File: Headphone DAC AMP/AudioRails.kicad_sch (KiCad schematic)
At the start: 35 parts, among them U12 TPS74501PDRVR, U14 ADP7185ACPZN-R7, U2 TPS7A39

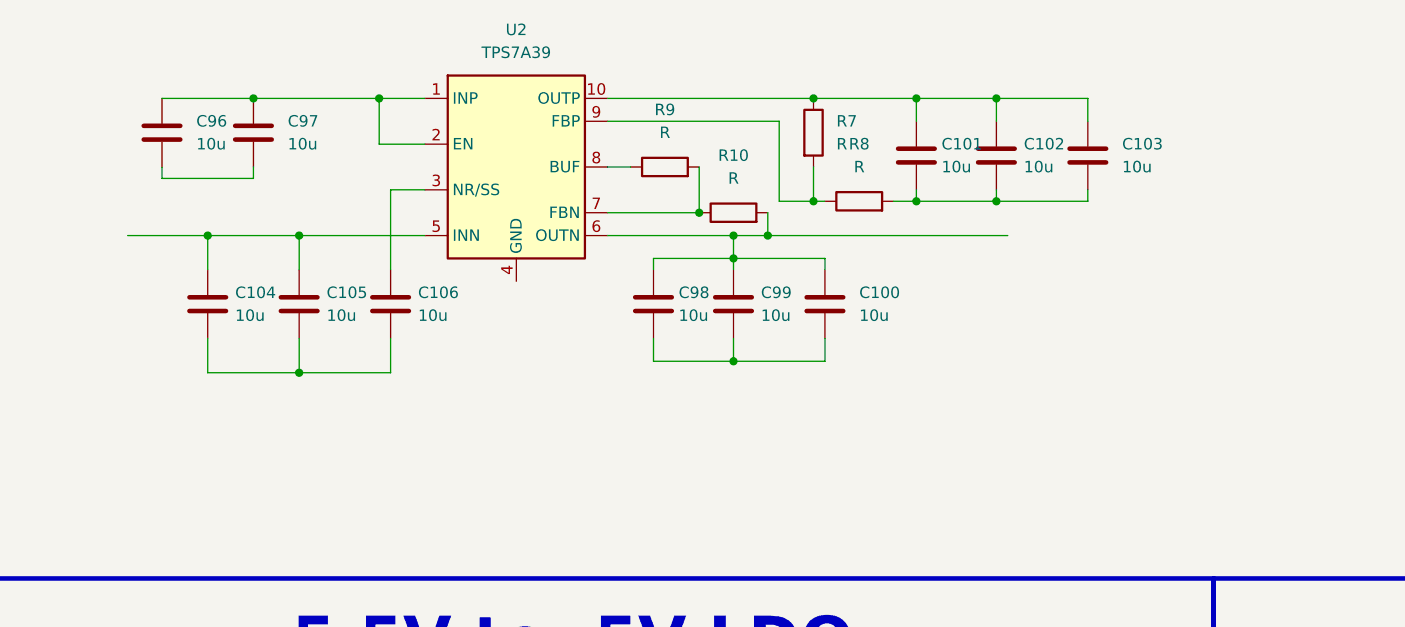
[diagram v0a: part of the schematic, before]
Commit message: Update schematic connections and add backup files
Added new junctions and wires to AudioRails.kicad_sch, updated connections for improved signal routing, and removed/re-added backup zip files. Also updated related schematic files to reflect new connections and organization.
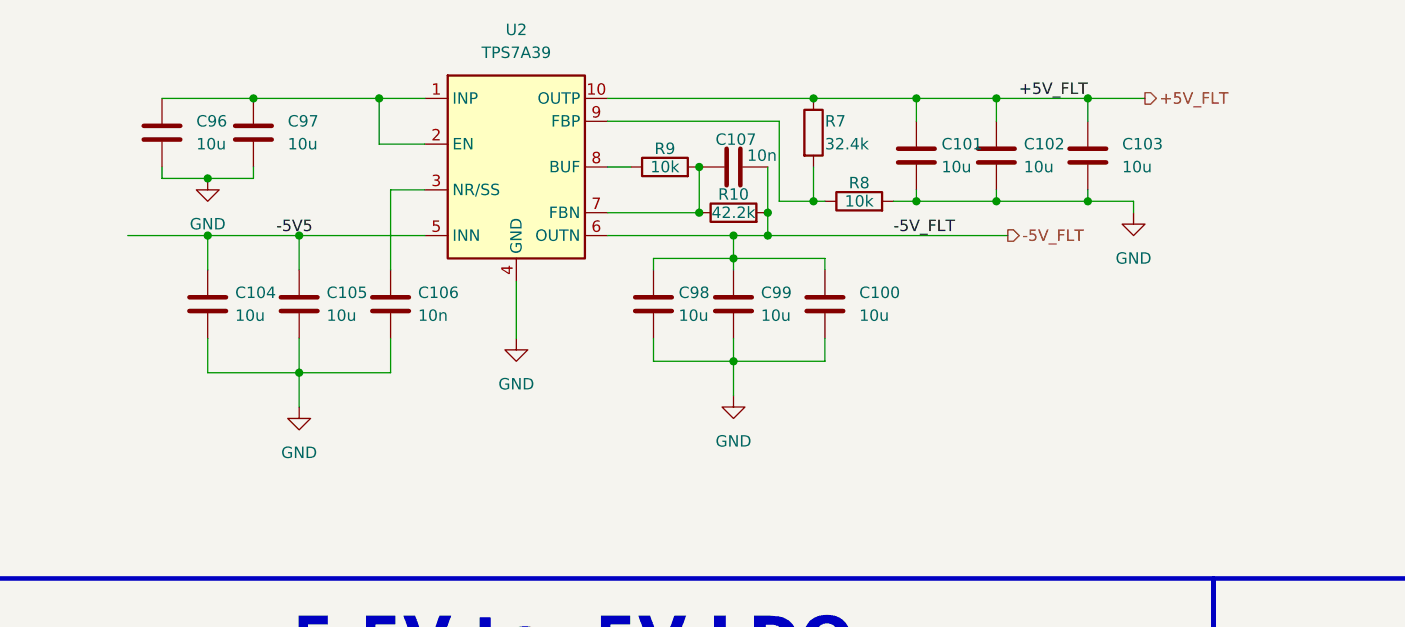
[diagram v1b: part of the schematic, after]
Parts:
- added C107: 10n, Capacitor_SMD:C_0603_1608Metric_Pad1.08x0.95mm_HandSolder, symbol Device:C
- C106: value 10u -> 10n
- R10: value R -> 42.2k
- R7: value R -> 32.4k
- R8, R9: value R -> 10k
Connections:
- net +5V_FLT: now also C101.1, C102.1, C103.1, R7.1, U2.10 (OUTP)
- net -5V5: now also C104.1, C105.1, U2.5 (INN)
- net -5V_FLT: now also C100.1, C98.1, C99.1, R10.2, U2.6 (OUTN), C107.2
- net GND: now also C100.2, C101.2, C102.2, C103.2, C104.2, C105.2, C106.2, C96.2, C97.2, C98.2, C99.2, R8.2, U2.11 (GND), U2.4 (GND)
- net at R10.1, R9.2, U2.7 (FBN): now also C107.1

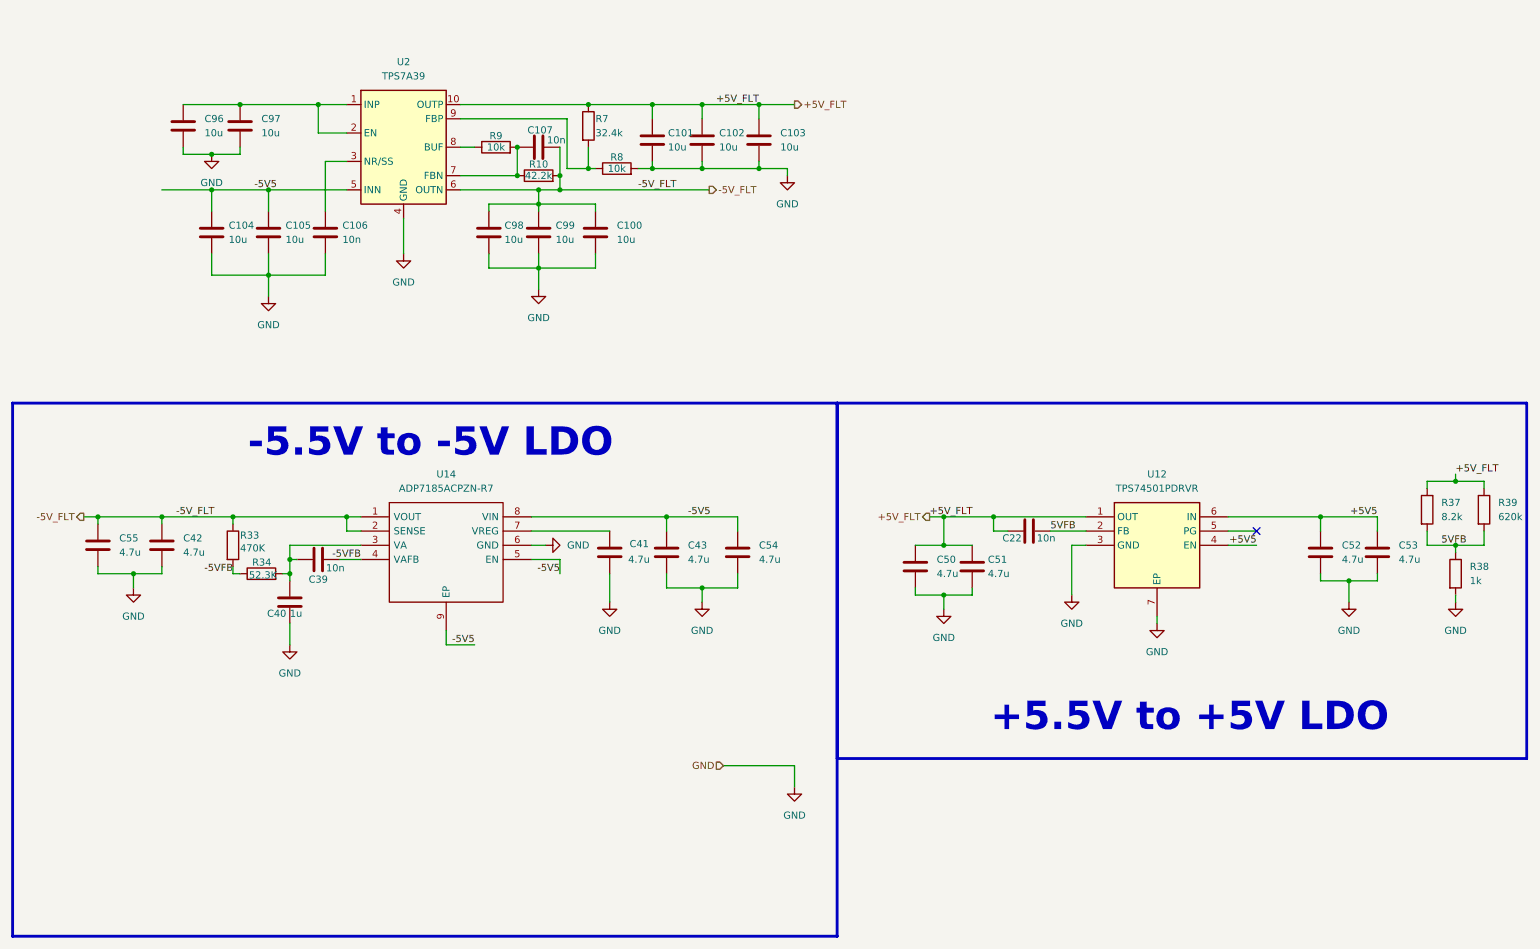
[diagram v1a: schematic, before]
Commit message: Refactor AudioRails schematic for new LDO and layout
Removed ADP7185 and TPS74501 LDO symbols and related wiring, updated power rail text to '+-6V to +-5V LDO', and significantly simplified the schematic layout and wiring by replacing the two seperate regulators with a single TPS7A39.
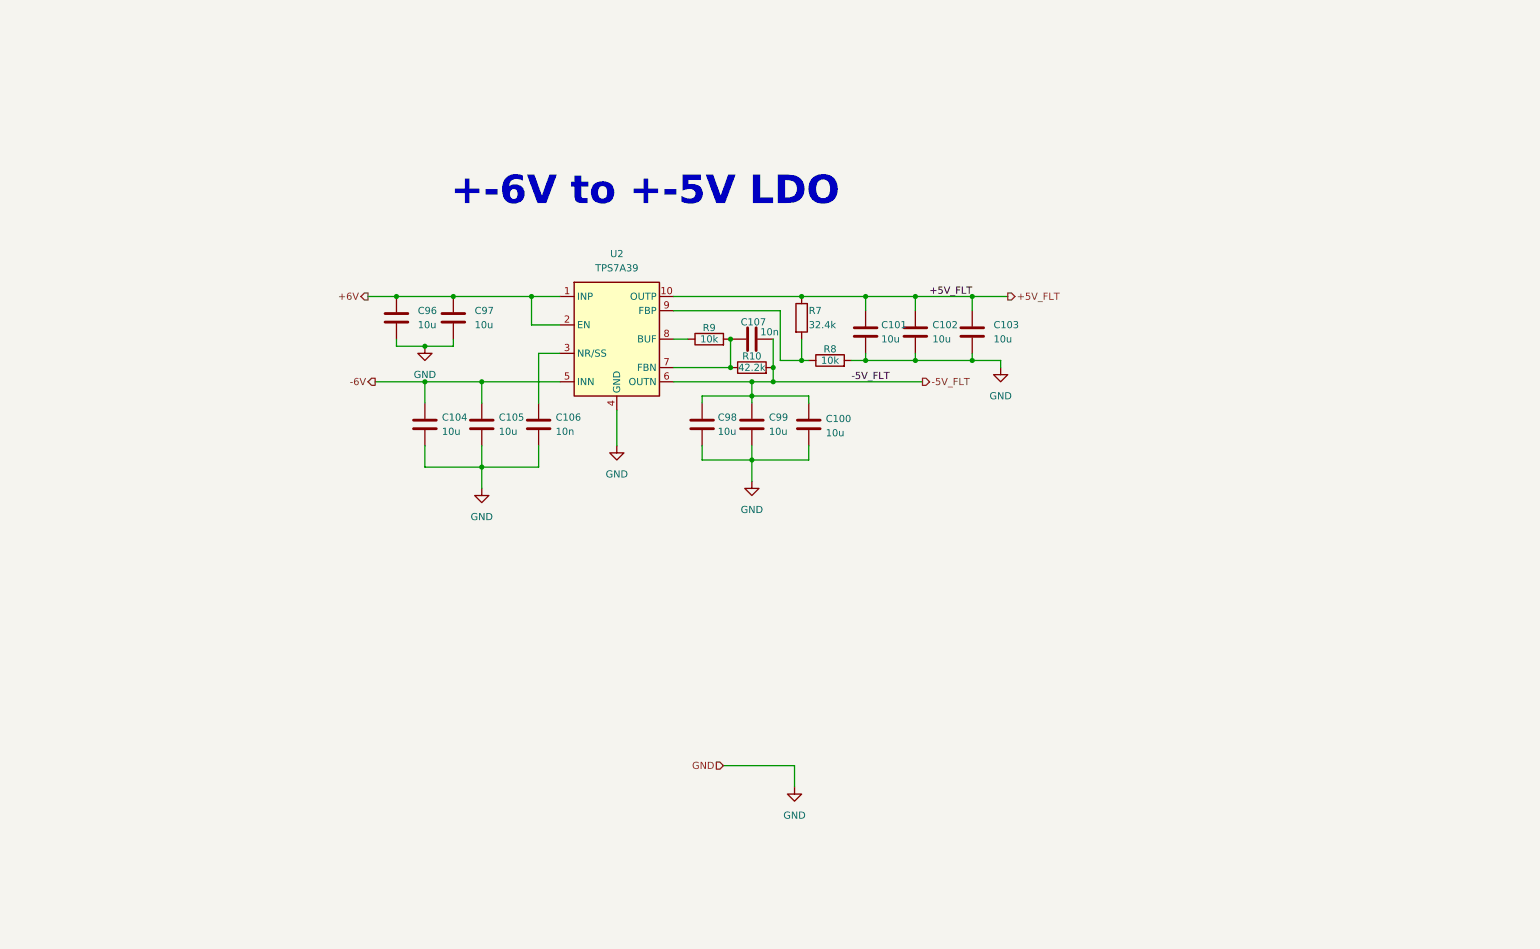
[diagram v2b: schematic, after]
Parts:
- removed C22, C39: 10n, Capacitor_SMD:C_0402_1005Metric_Pad0.74x0.62mm_HandSolder, symbol Device:C
- removed C40: 1u, Capacitor_SMD:C_0603_1608Metric_Pad1.08x0.95mm_HandSolder, symbol Device:C
- removed C41, C42, C43, C50, C51, C52, C53, C54, C55: 4.7u, Capacitor_SMD:C_0603_1608Metric_Pad1.08x0.95mm_HandSolder, symbol Device:C
- removed R33: 470K, Resistor_SMD:R_0805_2012Metric_Pad1.20x1.40mm_HandSolder, symbol Device:R
- removed R34: 52.3K, Resistor_SMD:R_0805_2012Metric_Pad1.20x1.40mm_HandSolder, symbol Device:R
- removed R37: 8.2k, Resistor_SMD:R_0805_2012Metric_Pad1.20x1.40mm_HandSolder, symbol Device:R
- removed R38: 1k, Resistor_SMD:R_0805_2012Metric_Pad1.20x1.40mm_HandSolder, symbol Device:R
- removed R39: 620k, Resistor_SMD:R_0805_2012Metric_Pad1.20x1.40mm_HandSolder, symbol Device:R
- removed U12: TPS74501PDRVR, TPS74501PDRVR:SON65P200X200X80-7N, symbol TPS74501PDRVR:TPS74501PDRVR
- removed U14: ADP7185ACPZN-R7, ADP7185ACPZN-R7:SON50P200X200X60-9N, symbol ADP7185ACPZN-R7:ADP7185ACPZN-R7
- R10, R7, R8, R9: footprint (none) -> Resistor_SMD:R_0805_2012Metric
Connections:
- net +6V: now reaches C96.1, C97.1, U2.1 (INP), U2.2 (EN)
- net -5V5 renamed -6V
- no-connect marks 1 -> 0
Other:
- note added: "+-6V to +-5V LDO"
- note removed: "+5.5V to +5V LDO"
- note removed: "-5.5V to -5V LDO"
- moved on the sheet: C100, C101, C102, C103, C104, C105, C106, C107, C96, C97, C98, C99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

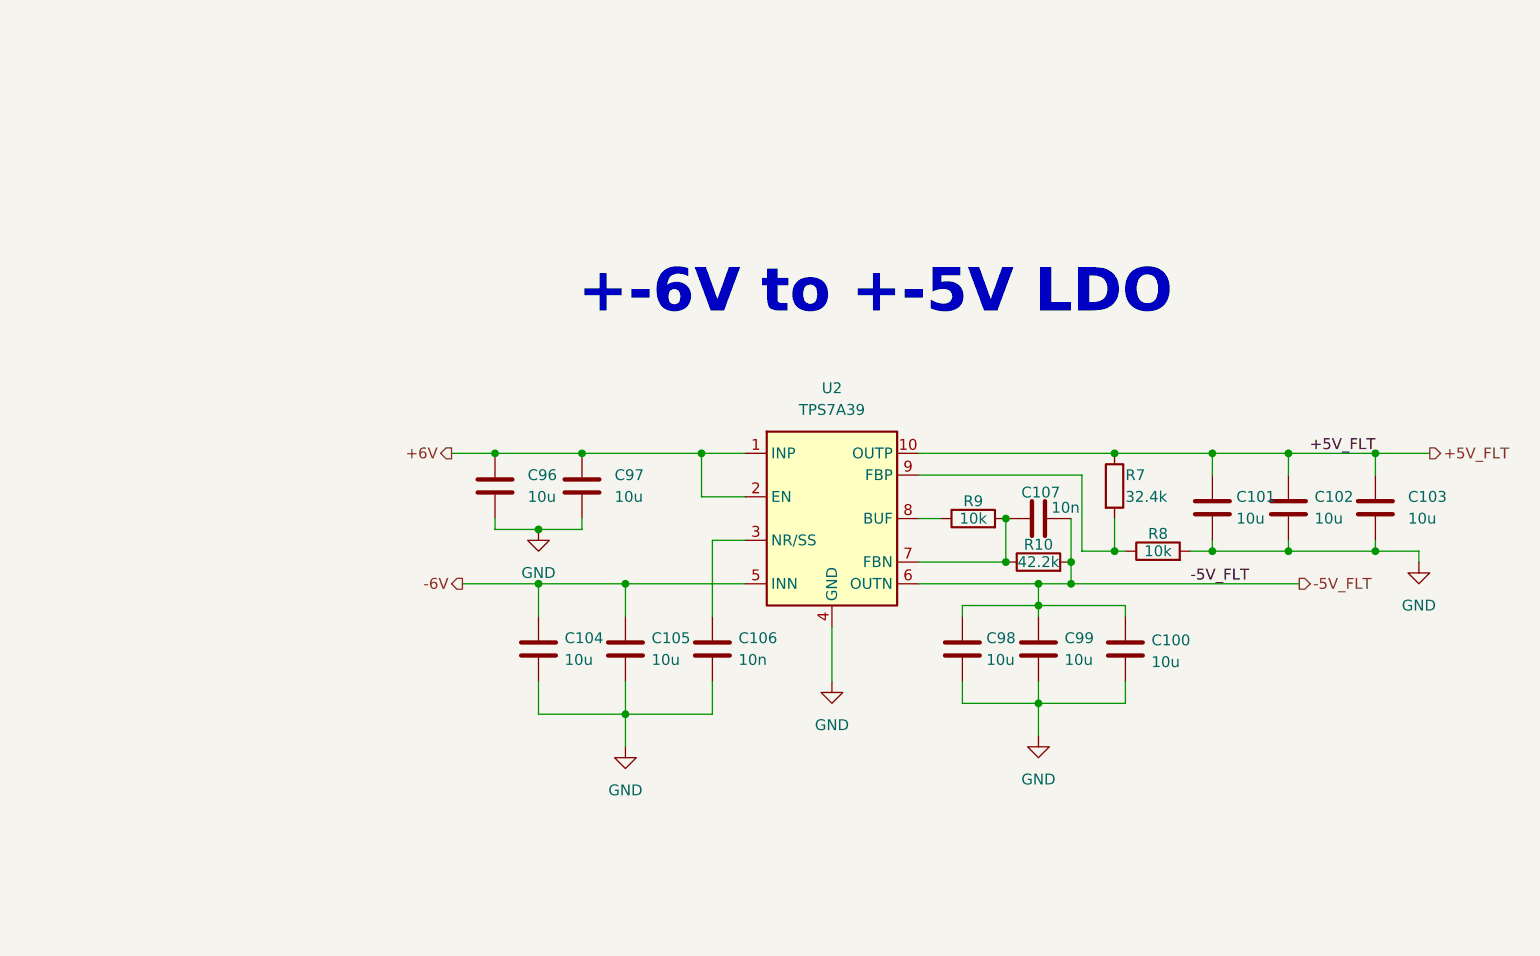
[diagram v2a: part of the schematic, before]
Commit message: dID lAYOUT FOR THE DIFFERENTIAL OUTPUT RAILS
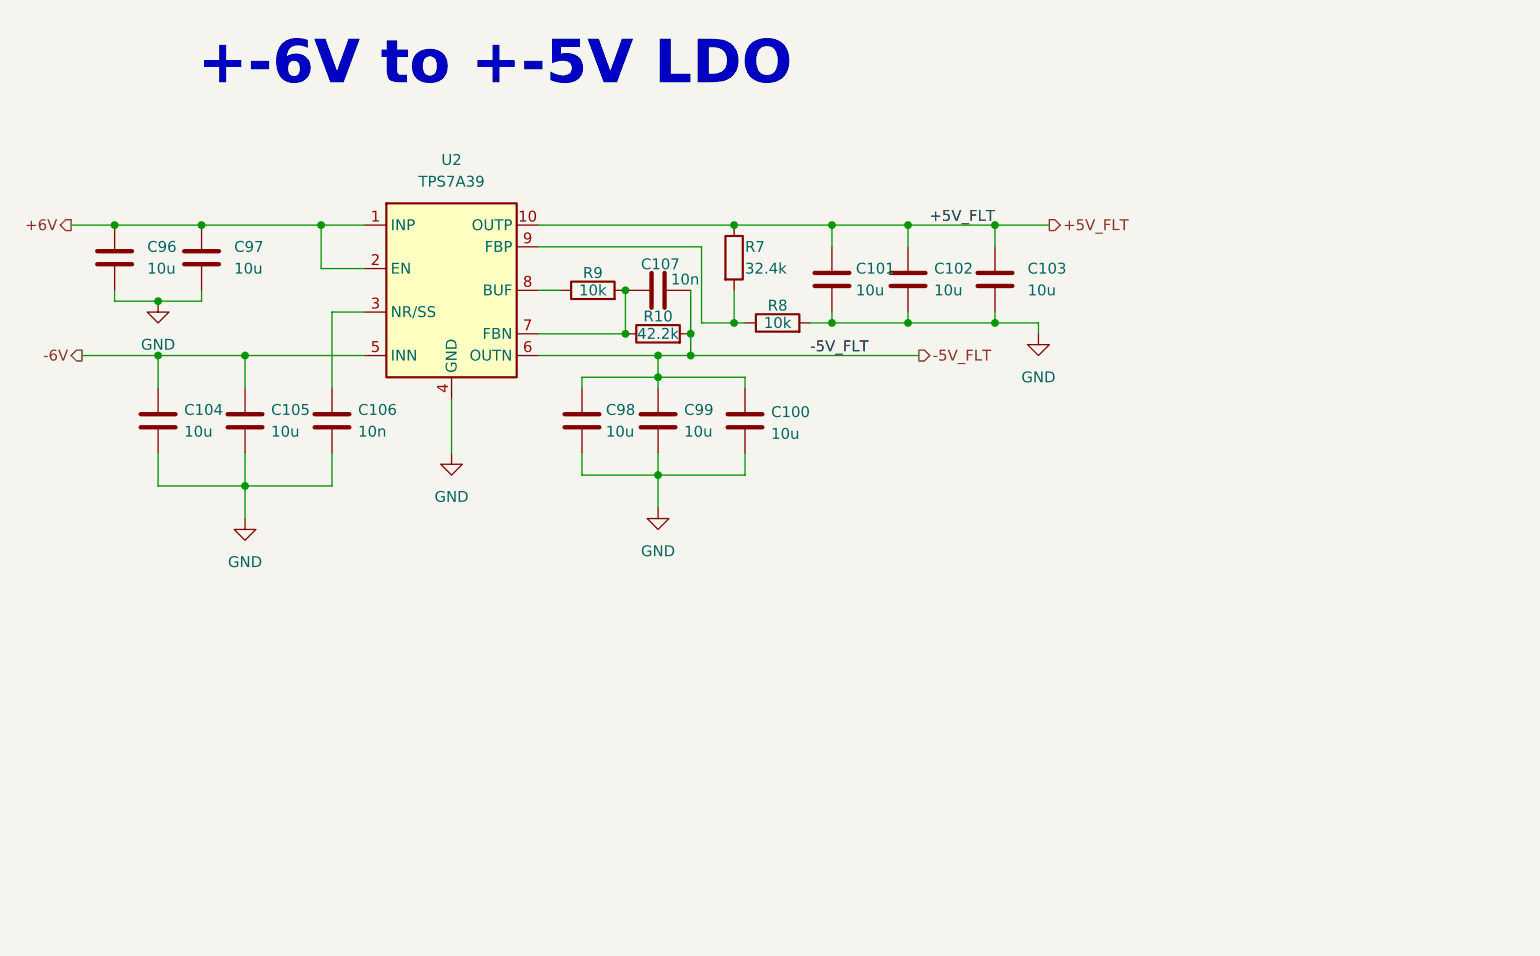
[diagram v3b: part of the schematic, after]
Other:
- moved on the sheet: C100, C101, C102, C103, C104, C105, C106, C107, C96, C97, C98, C99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
